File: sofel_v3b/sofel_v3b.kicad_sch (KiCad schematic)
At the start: 75 parts, among them J1 Pimaroni Trackball, J2 4PIN, J3 OLED, SW1 SW_PUSH_LED, SW10 SW_PUSH_LED, SW11 SW_PUSH_LED, SW12 SW_PUSH_LED, SW13 SW_PUSH_LED, SW14 SW_PUSH_LED, SW15 SW_PUSH_LED, SW16 SW_PUSH_LED, SW17 SW_PUSH_LED, SW18 SW_PUSH_LED, SW19 SW_PUSH_LED, SW2 SW_PUSH_LED, SW20 SW_PUSH_LED, SW21 SW_PUSH_LED, SW22 SW_PUSH_LED, SW23 SW_PUSH_LED, SW24 SW_PUSH_LED, SW25 Rotary_Encoder_Switch, SW26 SW_PUSH_LED, SW27 SW_PUSH_LED, SW28 SW_PUSH_LED, SW29 SW_PUSH_LED, SW3 SW_PUSH_LED, SW30 SW_PUSH_LED, SW4 SW_PUSH_LED, SW5 SW_PUSH_LED, SW6 SW_PUSH_LED, SW7 SW_PUSH_LED, SW8 SW_PUSH_LED, SW9 SW_PUSH_LED, U2 SN74AHCT1G125, U3 Pico

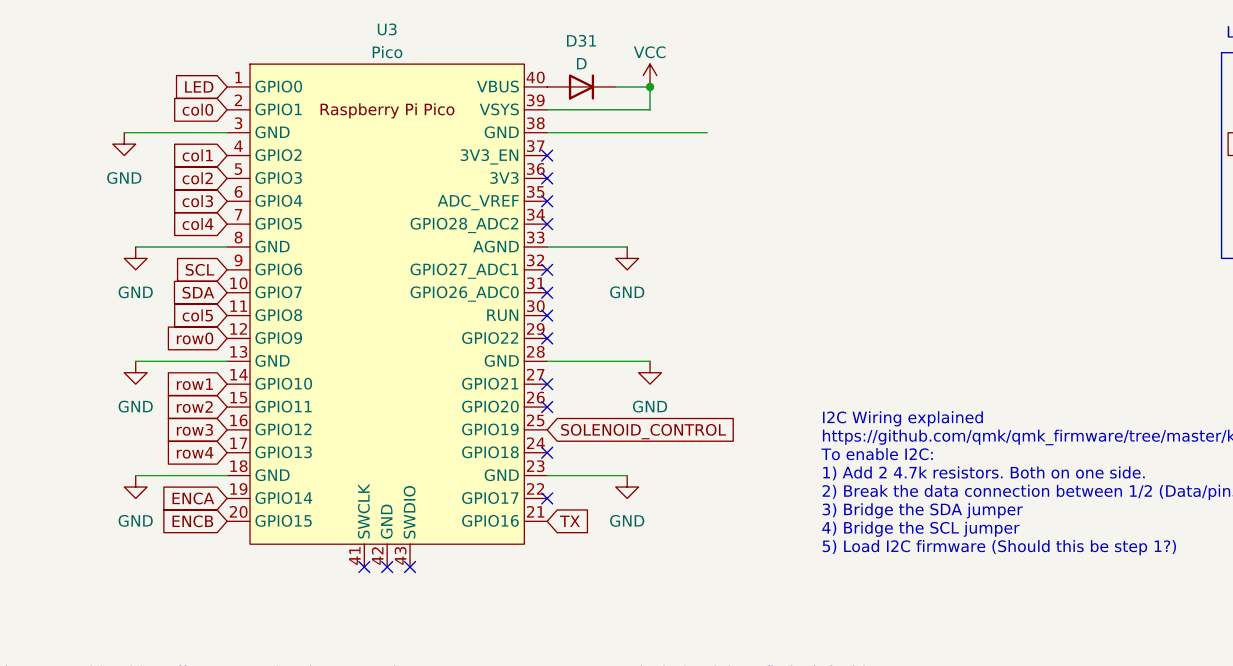
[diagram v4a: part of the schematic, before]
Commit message: V3.02 to V3.03 revisions Updated pico footrpint to flip MCU Fixed swapped oled pins Fixed MCU button holes
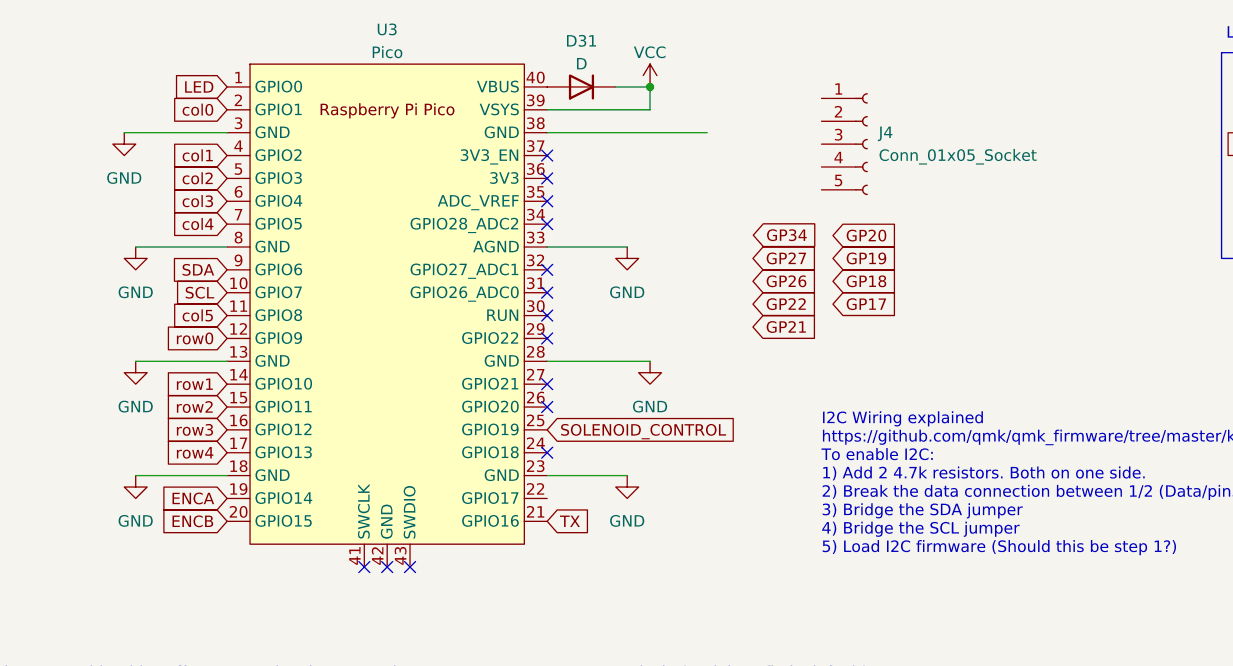
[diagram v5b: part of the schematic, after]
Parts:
- added J4: Conn_01x05_Socket, symbol Connector:Conn_01x05_Socket
- U3: footprint sofle_v3b:RPi_Pico_SMD_TH - Junco -DS Sofle v3b v3 -> sofle_v3b:RPi_Pico_SMD_TH - Junco -DS Sofle v3b v4
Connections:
- net SCL: now also U3.10 (GPIO7); no longer U3.9 (GPIO6)
- net SDA: now also U3.9 (GPIO6); no longer U3.10 (GPIO7)
- no-connect marks 18 -> 17
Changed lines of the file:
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@@
   )
   (no_connect (at 62.23 49.53))
-  (no_connect (at 62.23 41.91))
   (no_connect (at 62.23 57.15))
   (no_connect (at 62.23 46.99))
@@
   (no_connect (at 62.23 31.75))
   (no_connect (at 76.2 140.97))
+  (no_connect (at 62.23 41.91))
   (no_connect (at 62.23 54.61))
-  (no_connect (at 62.23 67.31))
   (no_connect (at 62.23 62.23))
   (no_connect (at 44.45 74.93))
@@
     )
   )
+  (global_label "GP26" (shape input) (at 85.09 43.18 0) (fields_autoplaced)
+    (effects (font (size 1.27 1.27)) (justify left))
+    (property "Intersheetrefs" "${INTERSHEET_REFS}" (at 92.3006 43.18 0)
+      (effects (font (size 1.27 1.27)) (justify left) hide)
+    )
+  )
   (global_label "row2" (shape input) (at 153.67 128.27 180)
     (effects (font (size 1.27 1.27)) (justify right))
@@
     )
   )
+  (global_label "GP18" (shape input) (at 93.98 43.18 0) (fields_autoplaced)
+    (effects (font (size 1.27 1.27)) (justify left))
+    (property "Intersheetrefs" "${INTERSHEET_REFS}" (at 101.1906 43.18 0)
+      (effects (font (size 1.27 1.27)) (justify left) hide)
+    )
+  )
   (global_label "col2" (shape input) (at 26.67 31.75 180)
     (effects (font (size 1.27 1.27)) (justify right))
@@
     )
   )
+  (global_label "GP27" (shape input) (at 85.09 40.64 0) (fields_autoplaced)
+    (effects (font (size 1.27 1.27)) (justify left))
+    (property "Intersheetrefs" "${INTERSHEET_REFS}" (at 92.3006 40.64 0)
+      (effects (font (size 1.27 1.27)) (justify left) hide)
+    )
+  )
   (global_label "col4" (shape input) (at 26.67 36.83 180)
     (effects (font (size 1.27 1.27)) (justify right))
@@
     )
   )
+  (global_label "GP22" (shape input) (at 85.09 45.72 0) (fields_autoplaced)
+    (effects (font (size 1.27 1.27)) (justify left))
+    (property "Intersheetrefs" "${INTERSHEET_REFS}" (at 92.3006 45.72 0)
+      (effects (font (size 1.27 1.27)) (justify left) hide)
+    )
+  )
   (global_label "row1" (shape input) (at 26.67 54.61 180)
     (effects (font (size 1.27 1.27)) (justify right))
@@
     )
   )
-  (global_label "SDA" (shape input) (at 26.67 44.45 180) (fields_autoplaced)
-    (effects (font (size 1.27 1.27)) (justify right))
-    (property "Intersheetrefs" "${INTERSHEET_REFS}" (at 20.8503 44.45 0)
-      (effects (font (size 1.27 1.27)) (justify right) hide)
-    )
-  )
   (global_label "ENCB" (shape input) (at 26.67 69.85 180)
     (effects (font (size 1.27 1.27)) (justify right))
@@
     )
   )
-  (global_label "SCL" (shape input) (at 26.67 41.91 180) (fields_autoplaced)
-    (effects (font (size 1.27 1.27)) (justify right))
-    (property "Intersheetrefs" "${INTERSHEET_REFS}" (at 20.9108 41.91 0)
-      (effects (font (size 1.27 1.27)) (justify right) hide)
-    )
-  )
   (global_label "col2" (shape input) (at 220.98 87.63 90)
     (effects (font (size 1.27 1.27)) (justify left))
@@
     )
   )
+  (global_label "GP19" (shape input) (at 93.98 40.64 0) (fields_autoplaced)
+    (effects (font (size 1.27 1.27)) (justify left))
+    (property "Intersheetrefs" "${INTERSHEET_REFS}" (at 101.1906 40.64 0)
+      (effects (font (size 1.27 1.27)) (justify left) hide)
+    )
+  )
   (global_label "row3" (shape input) (at 153.67 144.78 180)
     (effects (font (size 1.27 1.27)) (justify right))
@@
     )
   )
+  (global_label "GP20" (shape input) (at 93.98 38.1 0) (fields_autoplaced)
+    (effects (font (size 1.27 1.27)) (justify left))
+    (property "Intersheetrefs" "${INTERSHEET_REFS}" (at 101.1906 38.1 0)
+      (effects (font (size 1.27 1.27)) (justify left) hide)
+    )
+  )
+  (global_label "GP21" (shape input) (at 85.09 48.26 0) (fields_autoplaced)
+    (effects (font (size 1.27 1.27)) (justify left))
+    (property "Intersheetrefs" "${INTERSHEET_REFS}" (at 92.3006 48.26 0)
+      (effects (font (size 1.27 1.27)) (justify left) hide)
+    )
+  )
   (global_label "col1" (shape input) (at 26.67 29.21 180)
     (effects (font (size 1.27 1.27)) (justify right))
@@
     )
   )
+  (global_label "SCL" (shape input) (at 26.67 44.45 180) (fields_autoplaced)
+    (effects (font (size 1.27 1.27)) (justify right))
+    (property "Intersheetrefs" "${INTERSHEET_REFS}" (at 20.9108 44.45 0)
+      (effects (font (size 1.27 1.27)) (justify right) hide)
+    )
+  )
+  (global_label "GP34" (shape input) (at 85.1277 38.0572 0) (fields_autoplaced)
+    (effects (font (size 1.27 1.27)) (justify left))
+    (property "Intersheetrefs" "${INTERSHEET_REFS}" (at 92.3383 38.0572 0)
+      (effects (font (size 1.27 1.27)) (justify left) hide)
+    )
+  )
   (global_label "col3" (shape input) (at 200.66 87.63 90)
     (effects (font (size 1.27 1.27)) (justify left))
@@
     )
   )
+  (global_label "GP17" (shape input) (at 93.98 45.72 0) (fields_autoplaced)
+    (effects (font (size 1.27 1.27)) (justify left))
+    (property "Intersheetrefs" "${INTERSHEET_REFS}" (at 101.1906 45.72 0)
+      (effects (font (size 1.27 1.27)) (justify left) hide)
+    )
+  )
   (global_label "LED" (shape input) (at 143.51 27.94 180) (fields_autoplaced)
     (effects (font (size 1.27 1.27)) (justify right))
@@
     )
   )
+  (global_label "SDA" (shape input) (at 26.67 41.91 180) (fields_autoplaced)
+    (effects (font (size 1.27 1.27)) (justify right))
+    (property "Intersheetrefs" "${INTERSHEET_REFS}" (at 20.8503 41.91 0)
+      (effects (font (size 1.27 1.27)) (justify right) hide)
+    )
+  )
   (global_label "row1" (shape input) (at 153.67 111.76 180)
     (effects (font (size 1.27 1.27)) (justify right))
@@
       (effects (font (size 1.27 1.27)))
     )
-    (property "Footprint" "sofle_v3b:RPi_Pico_SMD_TH - Junco -DS Sofle v3b v3" (at 44.45 45.72 90)
+    (property "Footprint" "sofle_v3b:RPi_Pico_SMD_TH - Junco -DS Sofle v3b v4" (at 44.45 45.72 90)
       (effects (font (size 1.27 1.27)) hide)
     )
@@
         )
       )
+    )
+  )
+  (symbol (lib_id "Connector:Conn_01x05_Socket") (at 97.79 27.94 0) (unit 1)
+    (in_bom yes) (on_board yes) (dnp no) (fields_autoplaced)
+    (property "Reference" "J4" (at 99.06 26.67 0)
+      (effects (font (size 1.27 1.27)) (justify left))
+    )
+    (property "Value" "Conn_01x05_Socket" (at 99.06 29.21 0)
+      (effects (font (size 1.27 1.27)) (justify left))
+    )
+    (property "Footprint" "" (at 97.79 27.94 0)
+      (effects (font (size 1.27 1.27)) hide)
+    )
+    (property "Datasheet" "~" (at 97.79 27.94 0)
+      (effects (font (size 1.27 1.27)) hide)
+    )
+    (pin "1")
+    (pin "2")
+    (pin "3")
+    (pin "4")
+    (pin "5")
+    (instances
+      (project "sofel_v3b"
+        (path "/06057b3a-55ab-4f4e-913e-2aeec5ff3587"
+          (reference "J4") (unit 1)
+        )
+      )

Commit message: Improved led gnd markings reduced led tweezer hole size added markings for key plate post holes moved pimornoi traces
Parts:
- SW1, SW10, SW11, SW12, SW13, SW14, SW15, SW16, SW17, SW18, SW19, SW2, SW20, SW21, SW22, SW23, SW24, SW26, SW27, SW28, SW29, SW3, SW30, SW4, SW5, SW6, SW7, SW8, SW9: footprint sofle_v3b:Cherry_MX_DS_Hotswap_miniE_1U -> sofle_v3b:Cherry_MX_DS_Hotswap_miniE_1U_v3.03

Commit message: Added keyplate layer Added keyplate and backplate .step
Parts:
- TH1: footprint SofleChocLoud:Hole from sofle for M2 posts gold rimmer -> sofle_v3b:Hole from sofle for M2 posts gold rimmer
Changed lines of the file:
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@@
       (effects (font (size 1.524 1.524)))
     )
-    (property "Footprint" "SofleChocLoud:Hole from sofle for M2 posts gold rimmer" (at 19.05 190.5 0)
+    (property "Footprint" "sofle_v3b:Hole from sofle for M2 posts gold rimmer" (at 19.05 190.5 0)
       (effects (font (size 1.524 1.524)) hide)
     )

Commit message: Keyplate revisions fixed middle hole sizes created oled plate updated oled footprint with plate hole
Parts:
- TH1, TH2, TH7: footprint sofle_v3b:Hole from sofle for M2 posts gold rimmer -> sofle_v3b:Hole from sofle for M2 posts gold rimmer wide-keyplate-hole
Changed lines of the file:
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@@
       (effects (font (size 1.524 1.524)))
     )
-    (property "Footprint" "sofle_v3b:Hole from sofle for M2 posts gold rimmer" (at 19.05 190.5 0)
+    (property "Footprint" "sofle_v3b:Hole from sofle for M2 posts gold rimmer wide-keyplate-hole" (at 19.05 190.5 0)
       (effects (font (size 1.524 1.524)) hide)
     )
@@
       (effects (font (size 1.524 1.524)))
     )
-    (property "Footprint" "sofle_v3b:Hole from sofle for M2 posts gold rimmer" (at 27.94 190.5 0)
+    (property "Footprint" "sofle_v3b:Hole from sofle for M2 posts gold rimmer wide-keyplate-hole" (at 27.94 190.5 0)
       (effects (font (size 1.524 1.524)) hide)
     )
@@
       (effects (font (size 1.524 1.524)))
     )
-    (property "Footprint" "sofle_v3b:Hole from sofle for M2 posts gold rimmer" (at 80.01 190.5 0)
+    (property "Footprint" "sofle_v3b:Hole from sofle for M2 posts gold rimmer wide-keyplate-hole" (at 80.01 190.5 0)
       (effects (font (size 1.524 1.524)) hide)
     )
